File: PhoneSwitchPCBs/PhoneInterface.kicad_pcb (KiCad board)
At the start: 2 copper layers, 101.6 x 50.8 mm, 55 parts, among them J1 Interface, J2 6P2C, K1 EC2-5NU, K2 EC2-5NU, K3 EC2-5NU, K4 EC2-5NU, K5 EC2-5NU, Q1 PHPT61003PYX, Q2 PHPT61003NYX, Q3 XP231N02013R-G, Q4 XP231N02013R-G, Q5 XP231N02013R-G, Q6 XP231N02013R-G, U1 TCMD1000, U2 NL17SZ14DBVT1G

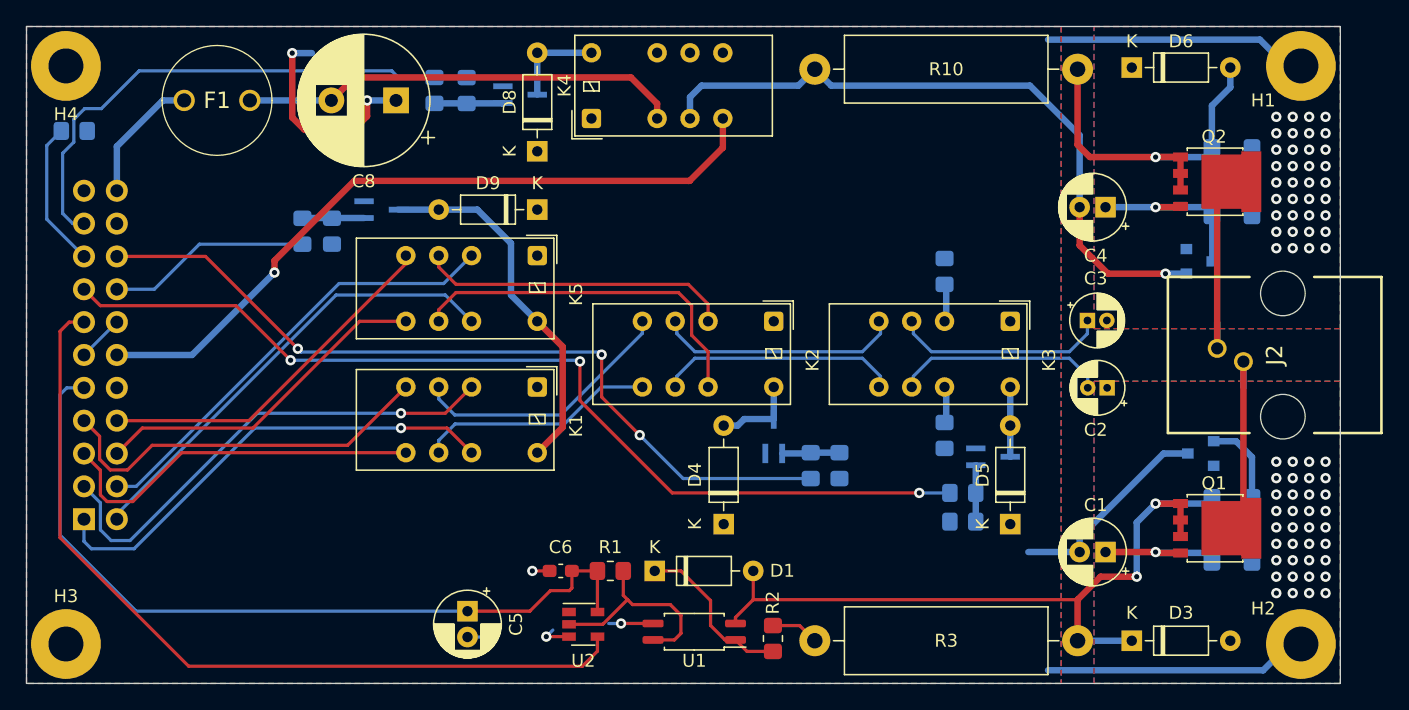
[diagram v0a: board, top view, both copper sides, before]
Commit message: Updated gerbers, added zip, added relay 3d model
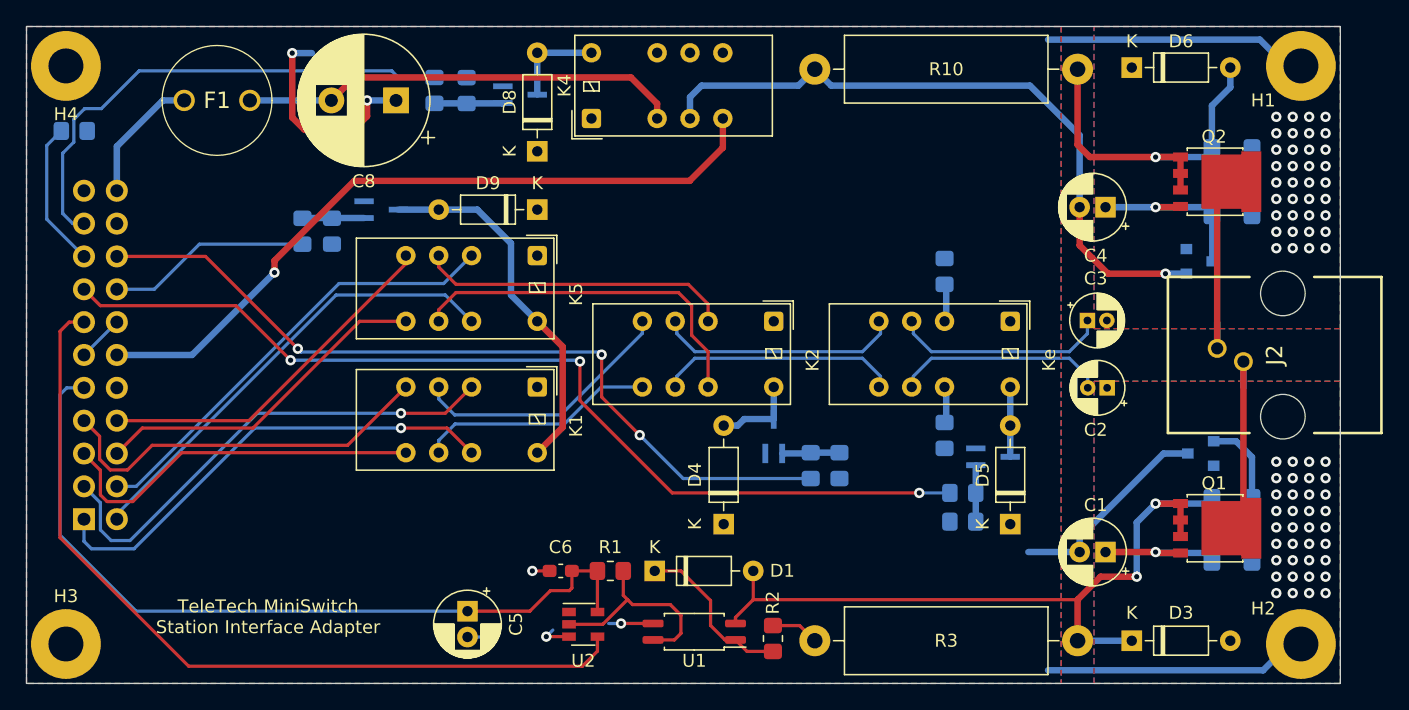
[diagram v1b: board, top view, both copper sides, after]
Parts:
- renumbered K3 to Ke
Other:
- board text added: "TeleTech MiniSwitch Station Interface Adapter"
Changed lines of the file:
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@@
   (general
     (thickness 1.6)
-    (drawings 4)
+    (drawings 5)
     (tracks 388)
     (zones 0)
@@
     (38 B.Mask user)
     (39 F.Mask user)
-    (40 Dwgs.User user hide)
+    (40 Dwgs.User user)
     (41 Cmts.User user)
     (42 Eco1.User user)
@@
     (visible_elements 7FFFFFFF)
     (pcbplotparams
-      (layerselection 0x010fc_ffffffff)
+      (layerselection 0x0d0fc_ffffffff)
       (usegerberextensions false)
       (usegerberattributes true)
@@
       (effects (font (size 1 1) (thickness 0.15)) (justify mirror))
     )
-    (fp_text user %R (at 0 0 270) (layer B.Fab)
-      (effects (font (size 0.5 0.5) (thickness 0.08)) (justify mirror))
-    )
     (fp_line (start 1.85 -0.95) (end -1.85 -0.95) (layer B.CrtYd) (width 0.05))
     (fp_line (start 1.85 0.95) (end 1.85 -0.95) (layer B.CrtYd) (width 0.05))
@@
     (fp_line (start -1 0.625) (end 1 0.625) (layer B.Fab) (width 0.1))
     (fp_line (start -1 -0.625) (end -1 0.625) (layer B.Fab) (width 0.1))
+    (fp_text user %R (at 0 0 270) (layer B.Fab)
+      (effects (font (size 0.5 0.5) (thickness 0.08)) (justify mirror))
+    )
     (pad 1 smd roundrect (at -1 0 270) (size 1.2 1.4) (layers B.Cu B.Paste B.Mask) (roundrect_rratio 0.2083325)
       (net 20 /RINGE))
@@
       (effects (font (size 0.8 0.8) (thickness 0.12)) (justify mirror))
     )
-    (pad 2 smd roundrect (at 1.55 0 180) (size 1.3 2.65) (layers B.Cu B.Paste B.Mask) (roundrect_rratio 0.1923076923076923)
+    (pad 2 smd roundrect (at 1.55 0 180) (size 1.3 2.65) (layers B.Cu B.Paste B.Mask) (roundrect_rratio 0.1923069230769231)
       (net 16 "Net-(D6-Pad2)"))
-    (pad 1 smd roundrect (at -1.55 0 180) (size 1.3 2.65) (layers B.Cu B.Paste B.Mask) (roundrect_rratio 0.1923076923076923)
+    (pad 1 smd roundrect (at -1.55 0 180) (size 1.3 2.65) (layers B.Cu B.Paste B.Mask) (roundrect_rratio 0.1923069230769231)
       (net 8 "Net-(C4-Pad1)"))
     (model ${KISYS3DMOD}/Resistor_SMD.3dshapes/R_1210_3225Metric.wrl
@@
       (effects (font (size 0.8 0.8) (thickness 0.12)) (justify mirror))
     )
-    (pad 2 smd roundrect (at 1.55 0 180) (size 1.3 2.65) (layers B.Cu B.Paste B.Mask) (roundrect_rratio 0.1923076923076923)
+    (pad 2 smd roundrect (at 1.55 0 180) (size 1.3 2.65) (layers B.Cu B.Paste B.Mask) (roundrect_rratio 0.1923069230769231)
       (net 8 "Net-(C4-Pad1)"))
-    (pad 1 smd roundrect (at -1.55 0 180) (size 1.3 2.65) (layers B.Cu B.Paste B.Mask) (roundrect_rratio 0.1923076923076923)
+    (pad 1 smd roundrect (at -1.55 0 180) (size 1.3 2.65) (layers B.Cu B.Paste B.Mask) (roundrect_rratio 0.1923069230769231)
       (net 5 /RING))
     (model ${KISYS3DMOD}/Resistor_SMD.3dshapes/R_1210_3225Metric.wrl
@@
       (effects (font (size 0.8 0.8) (thickness 0.12)) (justify mirror))
     )
-    (pad 2 smd roundrect (at 1.55 0 180) (size 1.3 2.65) (layers B.Cu B.Paste B.Mask) (roundrect_rratio 0.1923076923076923)
+    (pad 2 smd roundrect (at 1.55 0 180) (size 1.3 2.65) (layers B.Cu B.Paste B.Mask) (roundrect_rratio 0.1923069230769231)
       (net 2 "Net-(C1-Pad1)"))
-    (pad 1 smd roundrect (at -1.55 0 180) (size 1.3 2.65) (layers B.Cu B.Paste B.Mask) (roundrect_rratio 0.1923076923076923)
+    (pad 1 smd roundrect (at -1.55 0 180) (size 1.3 2.65) (layers B.Cu B.Paste B.Mask) (roundrect_rratio 0.1923069230769231)
       (net 4 /TIP))
     (model ${KISYS3DMOD}/Resistor_SMD.3dshapes/R_1210_3225Metric.wrl
@@
       (effects (font (size 0.8 0.8) (thickness 0.12)) (justify mirror))
     )
-    (pad 2 smd roundrect (at 1.55 0 180) (size 1.3 2.65) (layers B.Cu B.Paste B.Mask) (roundrect_rratio 0.1923076923076923)
+    (pad 2 smd roundrect (at 1.55 0 180) (size 1.3 2.65) (layers B.Cu B.Paste B.Mask) (roundrect_rratio 0.1923069230769231)
       (net 11 "Net-(D1-Pad2)"))
-    (pad 1 smd roundrect (at -1.55 0 180) (size 1.3 2.65) (layers B.Cu B.Paste B.Mask) (roundrect_rratio 0.1923076923076923)
+    (pad 1 smd roundrect (at -1.55 0 180) (size 1.3 2.65) (layers B.Cu B.Paste B.Mask) (roundrect_rratio 0.1923069230769231)
       (net 2 "Net-(C1-Pad1)"))
     (model ${KISYS3DMOD}/Resistor_SMD.3dshapes/R_1210_3225Metric.wrl
@@
       (rotate (xyz 0 0 0))
     )
+    (model ${KIPRJMOD}/PhoneInterfaceParts.pretty/EC2NU_KEM.step
+      (at (xyz 0 0 0))
+      (scale (xyz 1 1 1))
+      (rotate (xyz 0 0 0))
+    )
   )
   (module Relay_THT:Relay_DPDT_Kemet_EC2 (layer F.Cu)
@@
       (rotate (xyz 0 0 0))
     )
+    (model ${KIPRJMOD}/PhoneInterfaceParts.pretty/EC2NU_KEM.step
+      (at (xyz 0 0 0))
+      (scale (xyz 1 1 1))
+      (rotate (xyz 0 0 0))
+    )
   )
   (module Relay_THT:Relay_DPDT_Kemet_EC2 (layer F.Cu)
@@
     (descr "Kemet signal relay, DPDT, non-latching, single coil latching, https://content.kemet.com/datasheets/KEM_R7002_EC2_EE2.pdf")
     (tags "Kemet EC2 signal relay DPDT non single coil latching through hole THT")
-    (fp_text reference K3 (at 3 -3 270) (layer F.SilkS)
+    (fp_text reference Ke (at 3 -3 270) (layer F.SilkS)
       (effects (font (size 1 1) (thickness 0.15)))
     )
@@
       (rotate (xyz 0 0 0))
     )
+    (model ${KIPRJMOD}/PhoneInterfaceParts.pretty/EC2NU_KEM.step
+      (at (xyz 0 0 0))
+      (scale (xyz 1 1 1))
+      (rotate (xyz 0 0 0))
+    )
   )
   (module Relay_THT:Relay_DPDT_Kemet_EC2 (layer F.Cu)
@@
       (rotate (xyz 0 0 0))
     )
+    (model ${KIPRJMOD}/PhoneInterfaceParts.pretty/EC2NU_KEM.step
+      (at (xyz 0 0 0))
+      (scale (xyz 1 1 1))
+      (rotate (xyz 0 0 0))
+    )
   )
   (module Relay_THT:Relay_DPDT_Kemet_EC2 (layer F.Cu)
@@
       (rotate (xyz 0 0 0))
     )
+    (model ${KIPRJMOD}/PhoneInterfaceParts.pretty/EC2NU_KEM.step
+      (at (xyz 0 0 0))
+      (scale (xyz 1 1 1))
+      (rotate (xyz 0 0 0))
+    )
   )
   (module Imported_Parts:RJE0112001 (layer F.Cu)
@@
     )
   )
+  (gr_text "TeleTech MiniSwitch\nStation Interface Adapter" (at 111.0107 121.2088) (layer F.SilkS)
+    (effects (font (size 1 1) (thickness 0.15)))
+  )
   (gr_line (start 193.929 75.565) (end 92.329 75.565) (layer Edge.Cuts) (width 0.1))
